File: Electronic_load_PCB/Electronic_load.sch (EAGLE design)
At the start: 111 parts, among them IC7 LM1117IMPX-5.0, J1 XT60-M, J2 B2B-XH, J3 B4B-XH, J4 B2B-XH, J5 B2B-XH, J6 B2B-XH, J7 B2B-XH, J8 B5B-XH, Q1 IRFP250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

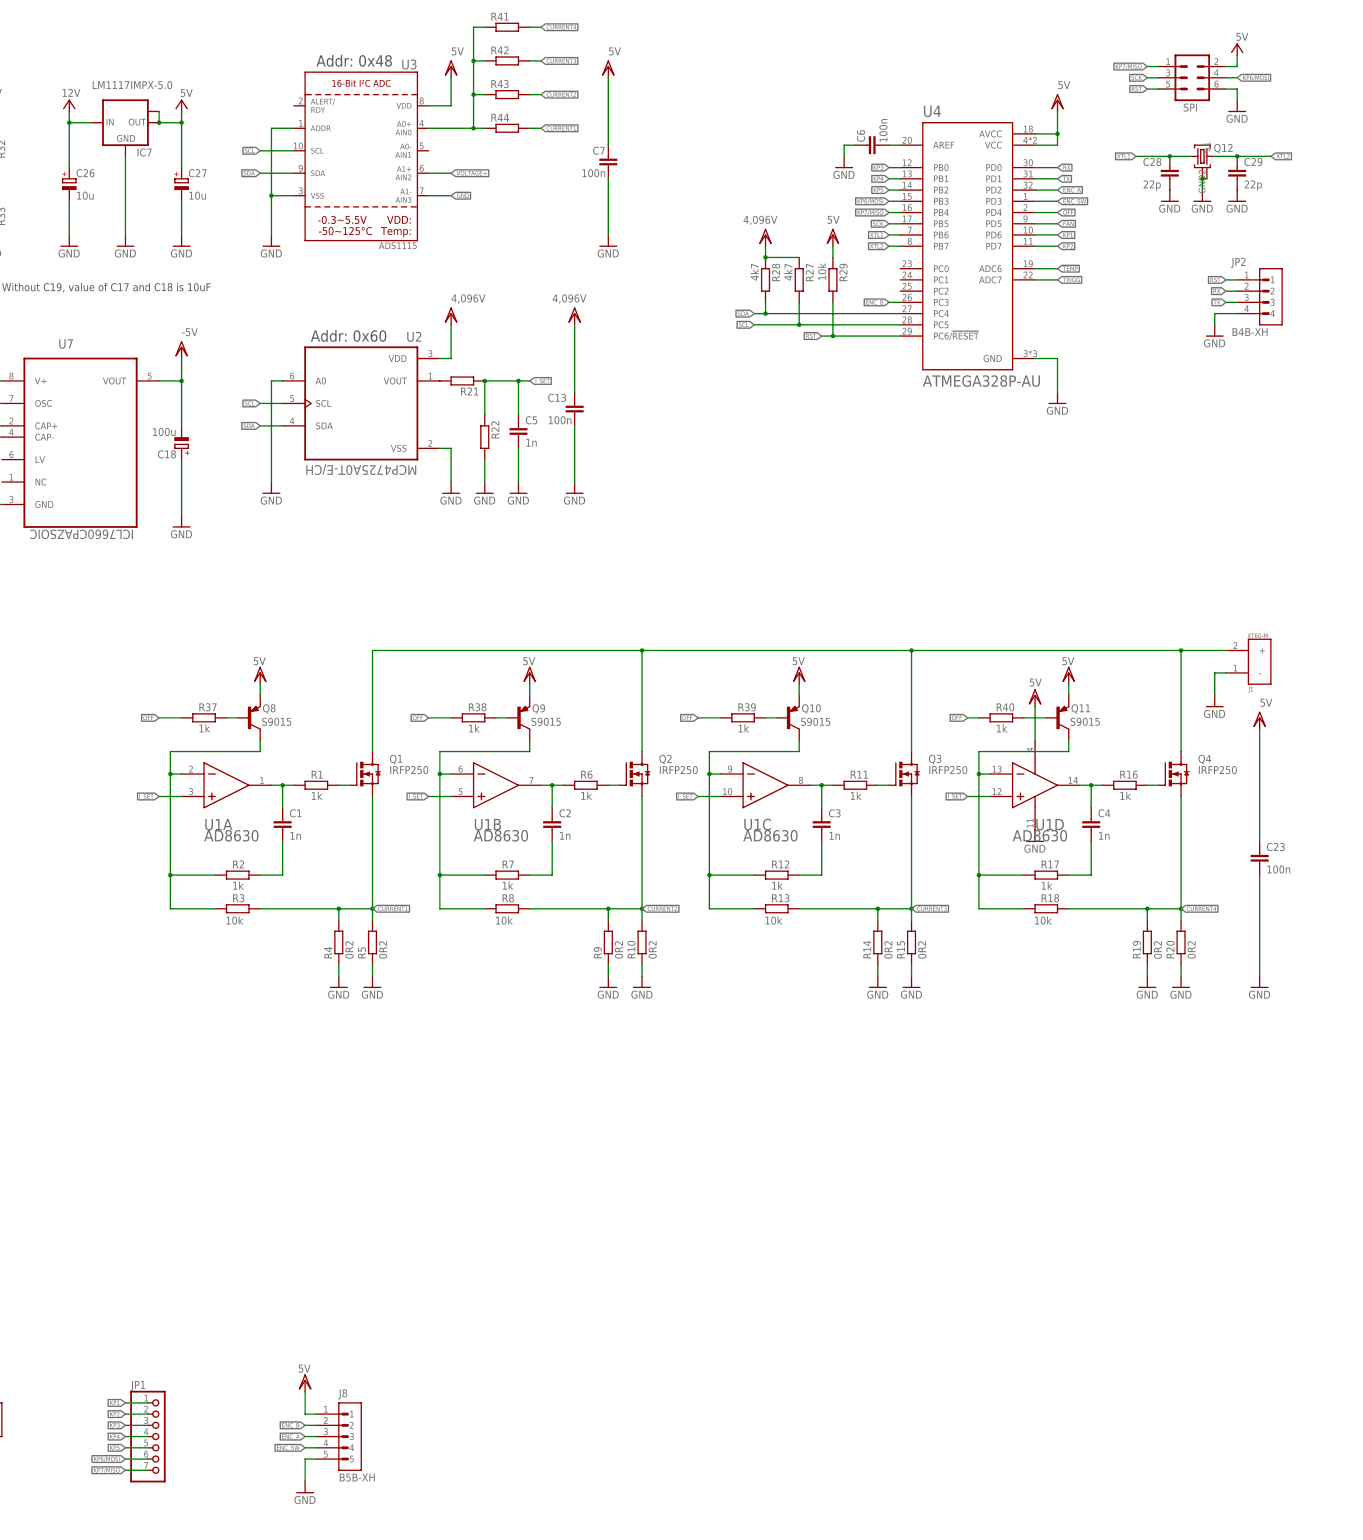
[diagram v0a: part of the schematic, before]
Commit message: 9 pin keypad
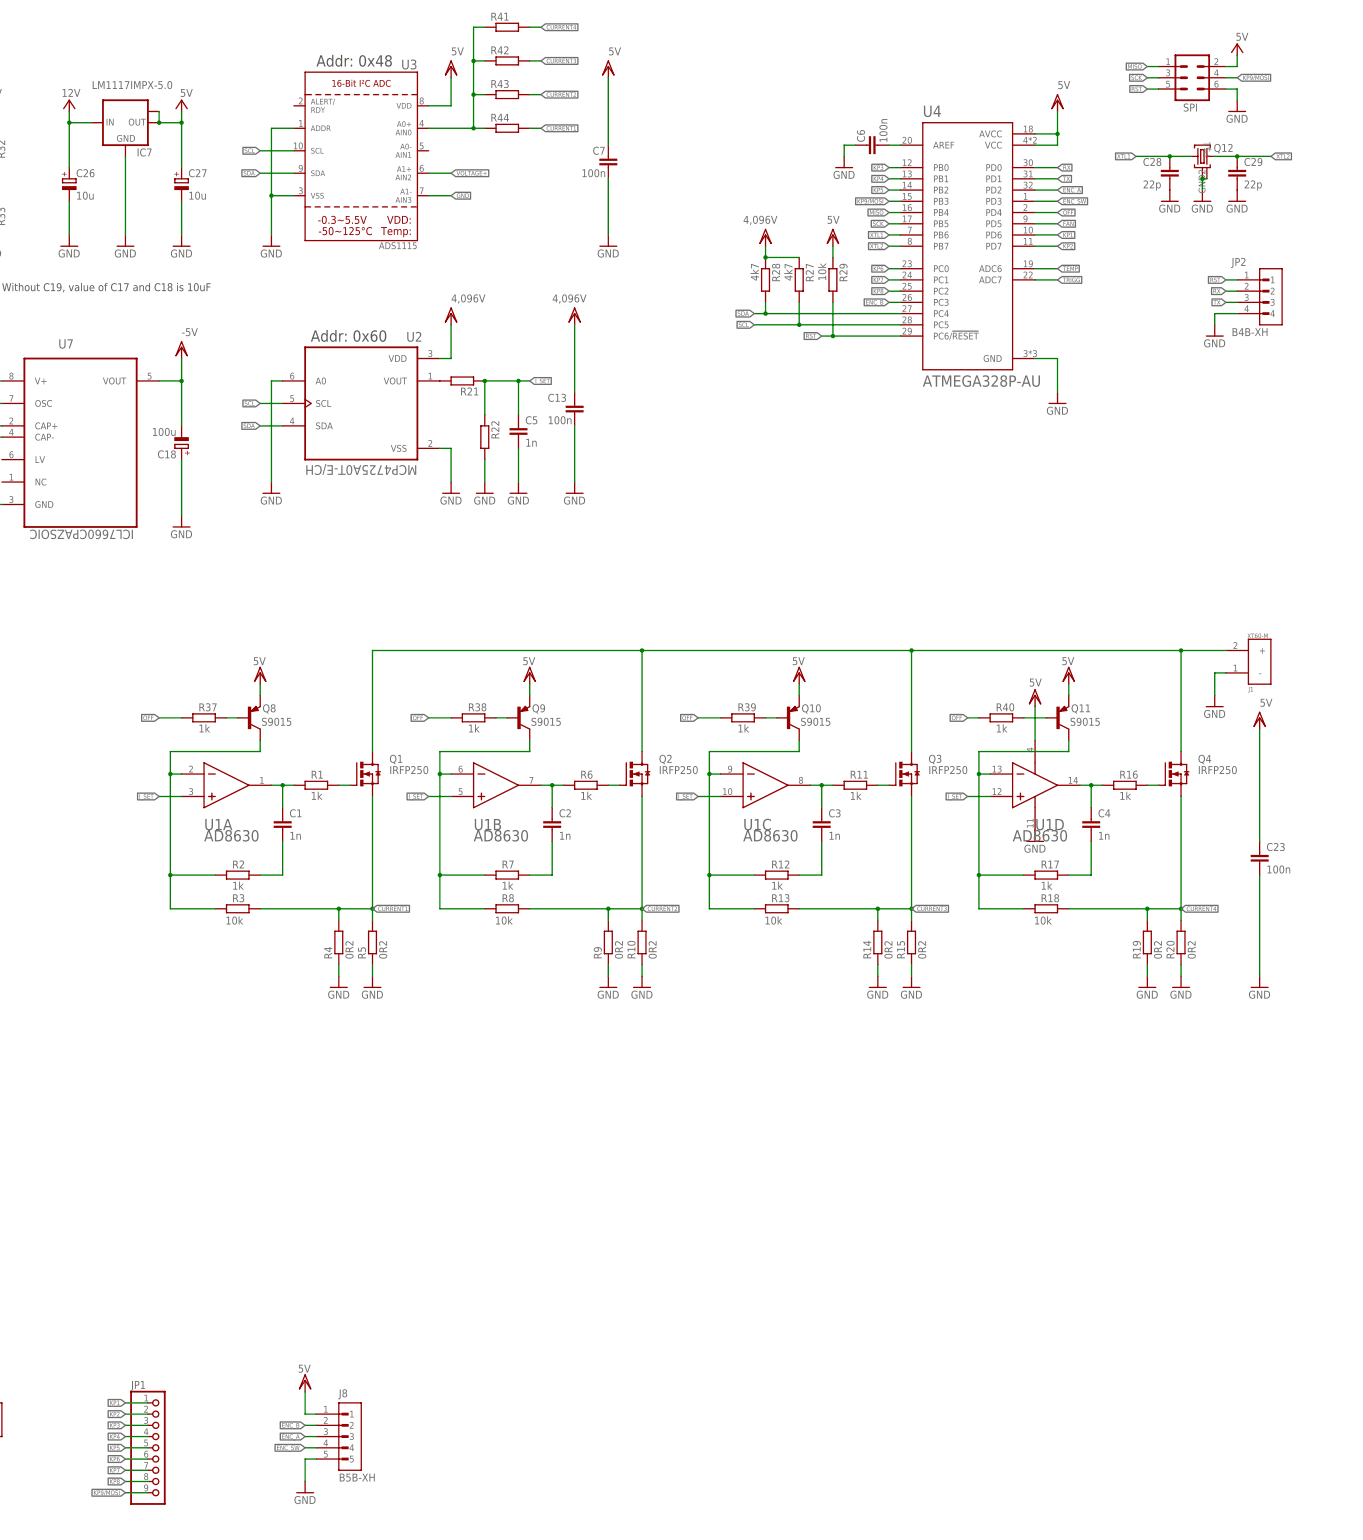
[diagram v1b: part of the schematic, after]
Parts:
- JP1: device pinhead:PINHD-1X7 -> pinhead:PINHD-1X9
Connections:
- removed net KP6/MOSI: JP1.6, SPI.4, U4.PB3
- removed net KP7/MISO: JP1.7, SPI.1, U4.PB4
- new net KP6: JP1.6, U4.PC0
- new net KP7: JP1.7, U4.PC1
- new net KP8: JP1.8, U4.PC2
- new net KP9/MOSI: JP1.9, SPI.4, U4.PB3
- new net MISO: SPI.1, U4.PB4
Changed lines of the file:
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@@
 <part name="GND50" library="supply1" library_urn="urn:adsk.eagle:library:371" deviceset="GND" device=""/>
 <part name="GND51" library="supply1" library_urn="urn:adsk.eagle:library:371" deviceset="GND" device=""/>
-<part name="JP1" library="pinhead" library_urn="urn:adsk.eagle:library:325" deviceset="PINHD-1X7" device="" package3d_urn="urn:adsk.eagle:package:22477/2"/>
 <part name="JP2" library="jst connectors" deviceset="B4B-XH" device="" package3d_urn="urn:adsk.eagle:package:36544612/2"/>
 <part name="GND52" library="supply1" library_urn="urn:adsk.eagle:library:371" deviceset="GND" device=""/>
@@
 <part name="R43" library="rcl" library_urn="urn:adsk.eagle:library:334" deviceset="R-EU_" device="R0603" package3d_urn="urn:adsk.eagle:package:23555/3"/>
 <part name="R44" library="rcl" library_urn="urn:adsk.eagle:library:334" deviceset="R-EU_" device="R0603" package3d_urn="urn:adsk.eagle:package:23555/3"/>
-<part name="U$3" library="voltage_references" deviceset="LM4140" device="" override_package3d_urn="urn:adsk.eagle:package:36704400/2" override_package_urn="urn:adsk.eagle:footprint:16321/1"/>
+<part name="U$3" library="voltage_references" deviceset="LM4140" device="" package3d_urn="urn:adsk.eagle:package:36503846/2" override_package3d_urn="urn:adsk.eagle:package:36704400/2" override_package_urn="urn:adsk.eagle:footprint:16321/1"/>
 <part name="C8" library="rcl" library_urn="urn:adsk.eagle:library:334" deviceset="CPOL-EU" device="CT3528" package3d_urn="urn:adsk.eagle:package:23325/2" value="10u"/>
 <part name="C9" library="rcl" library_urn="urn:adsk.eagle:library:334" deviceset="CPOL-EU" device="CT3216" package3d_urn="urn:adsk.eagle:package:23327/2" value="1u"/>
@@
 <part name="R29" library="rcl" library_urn="urn:adsk.eagle:library:334" deviceset="R-EU_" device="R0603" package3d_urn="urn:adsk.eagle:package:23555/3" value="10k"/>
 <part name="VDD30" library="supply1" library_urn="urn:adsk.eagle:library:371" deviceset="VDD" device=""/>
+<part name="JP1" library="pinhead" library_urn="urn:adsk.eagle:library:325" deviceset="PINHD-1X9" device="" package3d_urn="urn:adsk.eagle:package:22483/2"/>
 </parts>
 <sheets>
@@
 <wire x1="238.76" y1="226.06" x2="238.76" y2="269.24" width="0.1524" layer="90" style="longdash"/>
 <wire x1="238.76" y1="269.24" x2="200.66" y2="269.24" width="0.1524" layer="90" style="longdash"/>
-<wire x1="-121.92" y1="-71.12" x2="-96.52" y2="-71.12" width="0.1524" layer="90" style="longdash"/>
-<wire x1="-96.52" y1="-71.12" x2="-96.52" y2="-33.02" width="0.1524" layer="90" style="longdash"/>
+<wire x1="-121.92" y1="-73.66" x2="-96.52" y2="-73.66" width="0.1524" layer="90" style="longdash"/>
+<wire x1="-96.52" y1="-73.66" x2="-96.52" y2="-33.02" width="0.1524" layer="90" style="longdash"/>
 <wire x1="-96.52" y1="-33.02" x2="-121.92" y2="-33.02" width="0.1524" layer="90" style="longdash"/>
-<wire x1="-121.92" y1="-33.02" x2="-121.92" y2="-71.12" width="0.1524" layer="90" style="longdash"/>
+<wire x1="-121.92" y1="-33.02" x2="-121.92" y2="-73.66" width="0.1524" layer="90" style="longdash"/>
 <text x="-154.94" y="198.12" size="3.81" layer="90">Negative voltage generator</text>
 <wire x1="111.76" y1="238.76" x2="152.4" y2="238.76" width="0.1524" layer="90" style="shortdash"/>
@@
 <attribute name="VALUE" x="131.826" y="220.98" size="1.778" layer="96"/>
 </instance>
-<instance part="JP1" gate="A" x="-101.6" y="-55.88" smashed="yes">
-<attribute name="NAME" x="-107.95" y="-45.085" size="1.778" layer="95"/>
-<attribute name="VALUE" x="-107.95" y="-68.58" size="1.778" layer="96"/>
-</instance>
 <instance part="JP2" gate="G$1" x="147.32" y="200.66" smashed="yes">
 <attribute name="NAME" x="140.97" y="208.915" size="1.778" layer="95"/>
@@
 </instance>
 <instance part="VDD30" gate="G$1" x="50.8" y="215.9" smashed="yes"/>
+<instance part="JP1" gate="A" x="-101.6" y="-58.42" smashed="yes">
+<attribute name="NAME" x="-107.95" y="-45.085" size="1.778" layer="95"/>
+<attribute name="VALUE" x="-107.95" y="-73.66" size="1.778" layer="96"/>
+</instance>
 </instances>
 <busses>
@@
 <net name="KP1" class="0">
 <segment>
-<pinref part="JP1" gate="A" pin="1"/>
 <wire x1="-104.14" y1="-48.26" x2="-109.22" y2="-48.26" width="0.1524" layer="91"/>
 <label x="-109.22" y="-48.26" size="1.016" layer="95" rot="R180" xref="yes"/>
+<pinref part="JP1" gate="A" pin="1"/>
 </segment>
 <segment>
@@
 <net name="KP2" class="0">
 <segment>
-<pinref part="JP1" gate="A" pin="2"/>
 <wire x1="-104.14" y1="-50.8" x2="-109.22" y2="-50.8" width="0.1524" layer="91"/>
 <label x="-109.22" y="-50.8" size="1.016" layer="95" rot="R180" xref="yes"/>
+<pinref part="JP1" gate="A" pin="2"/>
 </segment>
 <segment>
@@
 <net name="KP3" class="0">
 <segment>
-<pinref part="JP1" gate="A" pin="3"/>
 <wire x1="-104.14" y1="-53.34" x2="-109.22" y2="-53.34" width="0.1524" layer="91"/>
 <label x="-109.22" y="-53.34" size="1.016" layer="95" rot="R180" xref="yes"/>
+<pinref part="JP1" gate="A" pin="3"/>
 </segment>
 <segment>
@@
 <net name="KP4" class="0">
 <segment>
-<pinref part="JP1" gate="A" pin="4"/>
 <wire x1="-104.14" y1="-55.88" x2="-109.22" y2="-55.88" width="0.1524" layer="91"/>
 <label x="-109.22" y="-55.88" size="1.016" layer="95" rot="R180" xref="yes"/>
+<pinref part="JP1" gate="A" pin="4"/>
 </segment>
 <segment>
@@
 <net name="KP5" class="0">
 <segment>
-<pinref part="JP1" gate="A" pin="5"/>
 <wire x1="-104.14" y1="-58.42" x2="-109.22" y2="-58.42" width="0.1524" layer="91"/>
 <label x="-109.22" y="-58.42" size="1.016" layer="95" rot="R180" xref="yes"/>
+<pinref part="JP1" gate="A" pin="5"/>
 </segment>
 <segment>
@@
 <wire x1="142.24" y1="200.66" x2="139.7" y2="200.66" width="0.1524" layer="91"/>
 <label x="139.7" y="200.66" size="1.016" layer="95" rot="R180" xref="yes"/>
-</segment>
-</net>
-<net name="KP6/MOSI" class="0">
-<segment>
-<pinref part="U4" gate="G$1" pin="PB3"/>
-<wire x1="66.04" y1="223.52" x2="63.5" y2="223.52" width="0.1524" layer="91"/>
-<label x="63.5" y="223.52" size="1.016" layer="95" rot="R180" xref="yes"/>
-</segment>
-<segment>
-<pinref part="JP1" gate="A" pin="6"/>
-<wire x1="-104.14" y1="-60.96" x2="-109.22" y2="-60.96" width="0.1524" layer="91"/>
-<label x="-109.22" y="-60.96" size="1.016" layer="95" rot="R180" xref="yes"/>
-</segment>
-<segment>
-<pinref part="SPI" gate="1" pin="4"/>
-<wire x1="139.7" y1="251.46" x2="142.24" y2="251.46" width="0.1524" layer="91"/>
-<label x="142.24" y="251.46" size="1.016" layer="95" xref="yes"/>
-</segment>
-</net>
-<net name="KP7/MISO" class="0">
-<segment>
-<pinref part="U4" gate="G$1" pin="PB4"/>
-<wire x1="66.04" y1="220.98" x2="63.5" y2="220.98" width="0.1524" layer="91"/>
-<label x="63.5" y="220.98" size="1.016" layer="95" rot="R180" xref="yes"/>
-</segment>
-<segment>
-<pinref part="JP1" gate="A" pin="7"/>
-<wire x1="-104.14" y1="-63.5" x2="-109.22" y2="-63.5" width="0.1524" layer="91"/>
-<label x="-109.22" y="-63.5" size="1.016" layer="95" rot="R180" xref="yes"/>
-</segment>
-<segment>
-<pinref part="SPI" gate="1" pin="1"/>
-<wire x1="124.46" y1="254" x2="121.92" y2="254" width="0.1524" layer="91"/>
-<label x="121.92" y="254" size="1.016" layer="95" rot="R180" xref="yes"/>
 </segment>
 </net>
@@
 </segment>
 </net>
+<net name="KP7" class="0">
+<segment>
+<wire x1="-104.14" y1="-63.5" x2="-109.22" y2="-63.5" width="0.1524" layer="91"/>
+<label x="-109.22" y="-63.5" size="1.016" layer="95" rot="R180" xref="yes"/>
+<pinref part="JP1" gate="A" pin="7"/>
+</segment>
+<segment>
+<pinref part="U4" gate="G$1" pin="PC1"/>
+<wire x1="66.04" y1="205.74" x2="63.5" y2="205.74" width="0.1524" layer="91"/>
+<label x="63.5" y="205.74" size="1.016" layer="95" rot="R180" xref="yes"/>
+</segment>
+</net>
+<net name="KP6" class="0">
+<segment>
+<wire x1="-104.14" y1="-60.96" x2="-109.22" y2="-60.96" width="0.1524" layer="91"/>
+<label x="-109.22" y="-60.96" size="1.016" layer="95" rot="R180" xref="yes"/>
+<pinref part="JP1" gate="A" pin="6"/>
+</segment>
+<segment>
+<pinref part="U4" gate="G$1" pin="PC0"/>
+<wire x1="66.04" y1="208.28" x2="63.5" y2="208.28" width="0.1524" layer="91"/>
+<label x="63.5" y="208.28" size="1.016" layer="95" rot="R180" xref="yes"/>
+</segment>
+</net>
+<net name="MISO" class="0">
+<segment>
+<pinref part="U4" gate="G$1" pin="PB4"/>
+<wire x1="66.04" y1="220.98" x2="63.5" y2="220.98" width="0.1524" layer="91"/>
+<label x="63.5" y="220.98" size="1.016" layer="95" rot="R180" xref="yes"/>
+</segment>
+<segment>
+<pinref part="SPI" gate="1" pin="1"/>
+<wire x1="124.46" y1="254" x2="121.92" y2="254" width="0.1524" layer="91"/>
+<label x="121.92" y="254" size="1.016" layer="95" rot="R180" xref="yes"/>
+</segment>
+</net>
+<net name="KP8" class="0">
+<segment>
+<pinref part="U4" gate="G$1" pin="PC2"/>
+<wire x1="66.04" y1="203.2" x2="63.5" y2="203.2" width="0.1524" layer="91"/>
+<label x="63.5" y="203.2" size="1.016" layer="95" rot="R180" xref="yes"/>
+</segment>
+<segment>
+<pinref part="JP1" gate="A" pin="8"/>
+<wire x1="-104.14" y1="-66.04" x2="-109.22" y2="-66.04" width="0.1524" layer="91"/>
+<label x="-109.22" y="-66.04" size="1.016" layer="95" rot="R180" xref="yes"/>
+</segment>
+</net>
+<net name="KP9/MOSI" class="0">
+<segment>
+<pinref part="JP1" gate="A" pin="9"/>
+<wire x1="-104.14" y1="-68.58" x2="-109.22" y2="-68.58" width="0.1524" layer="91"/>
+<label x="-109.22" y="-68.58" size="1.016" layer="95" rot="R180" xref="yes"/>
+</segment>
+<segment>
+<pinref part="U4" gate="G$1" pin="PB3"/>
+<wire x1="66.04" y1="223.52" x2="63.5" y2="223.52" width="0.1524" layer="91"/>
+<label x="63.5" y="223.52" size="1.016" layer="95" rot="R180" xref="yes"/>
+</segment>
+<segment>
+<pinref part="SPI" gate="1" pin="4"/>
+<wire x1="139.7" y1="251.46" x2="142.24" y2="251.46" width="0.1524" layer="91"/>
+<label x="142.24" y="251.46" size="1.016" layer="95" xref="yes"/>
+</segment>
+</net>

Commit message: added missing component values
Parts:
- R21: value (none) -> 15k
- R22, R41, R42, R43, R44: value (none) -> 1k
- R30: value (none) -> 470R
- R32: value 1k -> 68k
- R33: value 1k -> 18k
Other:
- moved on the sheet: D7, J6, J7, J8, JP1, R34, R35, R36, U8
